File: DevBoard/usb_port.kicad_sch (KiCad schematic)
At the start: 134 parts, among them J401 TYPE-C 16PCB1.6 IP68, J402 I2CC logic analyzer, Q401 PGQ04N070, Q402 PGQ04N070, Q403 AO3401A, Q404 AO3401A, Q405 AO3400A, Q406 AO3400A, Q407 PGQ04N070, Q408 PGQ04N070, U401 TPS25751DREFR, U402 M24512-DFMC6TG, U403 BQ25756RRVR, U404 TPS62933DRLR, U405 TPD4S201TRGRRQ1

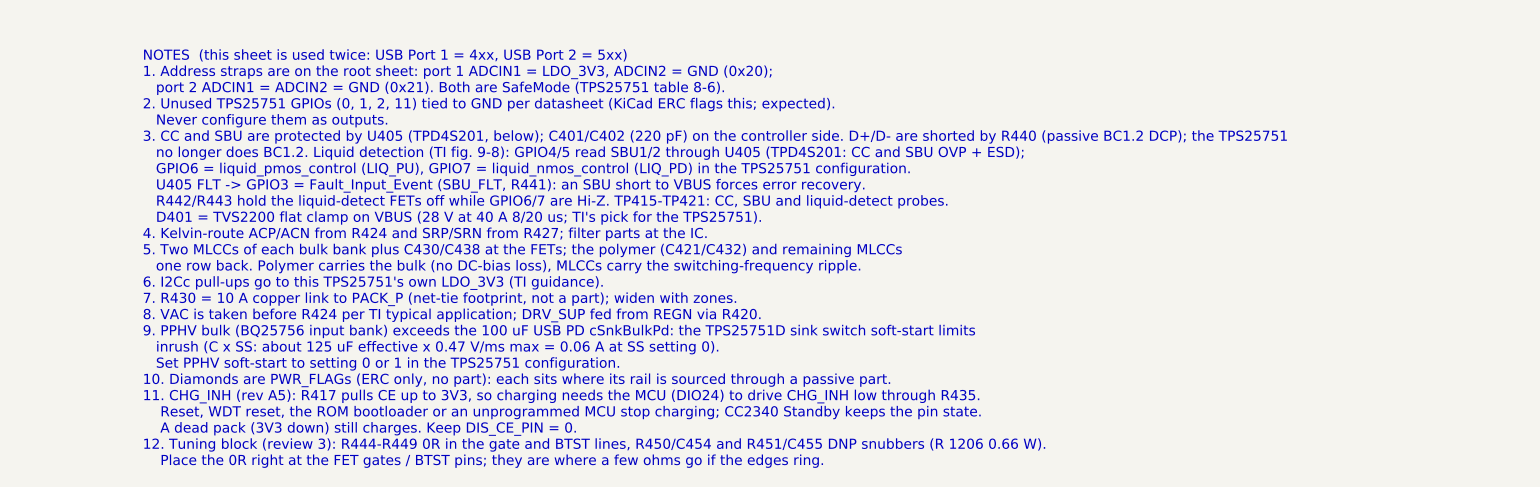
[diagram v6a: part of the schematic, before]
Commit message: Dev board: hybrid battery-side bulk, ship mode at 5 % SOC, CC2340 in stock
- C432/C532 (battery-side bulk, the only bulk cap biased in idle) ->
  Panasonic EEH-ZA1E101XP hybrid polymer (C264047), CP_Elec_6.3x7.7.
  Same 100 uF / 30 mOhm as the JIERR solid polymer, but leakage limit
  0.01CV = 25 uA instead of 0.2CV = 500 uA. +$1.28 per board. README
  item 43; review 4 B-4 closed. Board synced: 0 parity issues, no
  courtyard overlaps.
- Ship mode also triggers at RSOC <= 5 % (checklist, power states,
  review 4 S-1).
- CC2340R5MODA is in stock at TI.com (seen logged in, 2026-10-15):
  U301 Sourcing, bom_cost.py, checklist and README notes updated.

Co-Authored-By: Claude Opus 5.5 <noreply@anthropic.com>
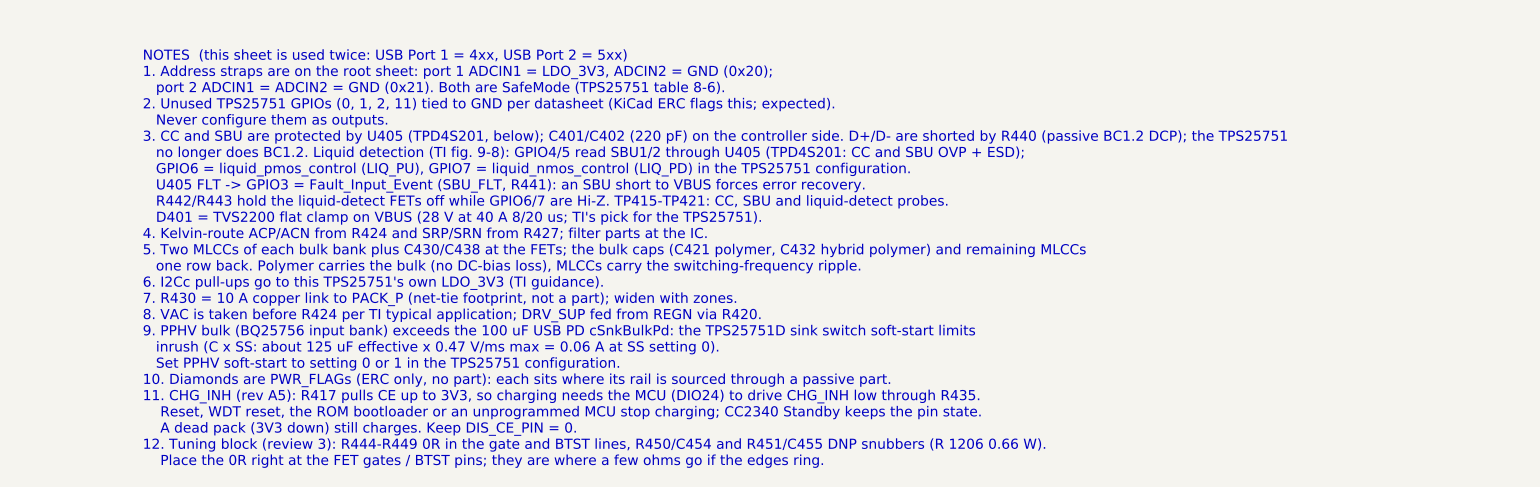
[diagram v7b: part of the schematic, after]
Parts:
- C432: footprint Capacitor_SMD:CP_Elec_6.3x5.8 -> Capacitor_SMD:CP_Elec_6.3x7.7; LCSC C46550465 -> C264047; MPN JIERR MA25V100M6x6 (polymer) -> Panasonic EEH-ZA1E101XP (hybrid polymer); Notes Battery-side bulk: solid polymer, no DC-bias loss (100 uF a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 -> Battery-side bulk (C432/C532): Panasonic ZA hybrid polymer 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
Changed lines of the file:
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@@
 		)
 	)
-	(text "NOTES  (this sheet is used twice: USB Port 1 = 4xx, USB Port 2 = 5xx)\n1. Address straps are on the root sheet: port 1 ADCIN1 = LDO_3V3, ADCIN2 = GND (0x20);\n   port 2 ADCIN1 = ADCIN2 = GND (0x21). Both are SafeMode (TPS25751 table 8-6).\n2. Unused TPS25751 GPIOs (0, 1, 2, 11) tied to GND per datasheet (KiCad ERC flags this; expected).\n   Never configure them as outputs.\n3. CC and SBU are protected by U405 (TPD4S201, below); C401/C402 (220 pF) on the controller side. D+/D- are shorted by R440 (passive BC1.2 DCP); the TPS25751\n   no longer does BC1.2. Liquid detection (TI fig. 9-8): GPIO4/5 read SBU1/2 through U405 (TPD4S201: CC and SBU OVP + ESD);\n   GPIO6 = liquid_pmos_control (LIQ_PU), GPIO7 = liquid_nmos_control (LIQ_PD) in the TPS25751 configuration.\n   U405 FLT -> GPIO3 = Fault_Input_Event (SBU_FLT, R441): an SBU short to VBUS forces error recovery.\n   R442/R443 hold the liquid-detect FETs off while GPIO6/7 are Hi-Z. TP415-TP421: CC, SBU and liquid-detect probes.\n   D401 = TVS2200 flat clamp on VBUS (28 V at 40 A 8/20 us; TI's pick for the TPS25751).\n4. Kelvin-route ACP/ACN from R424 and SRP/SRN from R427; filter parts at the IC.\n5. Two MLCCs of each bulk bank plus C430/C438 at the FETs; the polymer (C421/C432) and remaining MLCCs\n   one row back. Polymer carries the bulk (no DC-bias loss), MLCCs carry the switching-frequency ripple.\n6. I2Cc pull-ups go to this TPS25751's own LDO_3V3 (TI guidance).\n7. R430 = 10 A copper link to PACK_P (net-tie footprint, not a part); widen with zones.\n8. VAC is taken before R424 per TI typical application; DRV_SUP fed from REGN via R420.\n9. PPHV bulk (BQ25756 input bank) exceeds the 100 uF USB PD cSnkBulkPd: the TPS25751D sink switch soft-start limits\n   inrush (C x SS: about 125 uF effective x 0.47 V/ms max = 0.06 A at SS setting 0).\n   Set PPHV soft-start to setting 0 or 1 in the TPS25751 configuration.\n10. Diamonds are PWR_FLAGs (ERC only, no part): each sits where its rail is sourced through a passive part.\n11. CHG_INH (rev A5): R417 pulls CE up to 3V3, so charging needs the MCU (DIO24) to drive CHG_INH low through R435.\n    Reset, WDT reset, the ROM bootloader or an unprogrammed MCU stop charging; CC2340 Standby keeps the pin state.\n    A dead pack (3V3 down) still charges. Keep DIS_CE_PIN = 0.\n12. Tuning block (review 3): R444-R449 0R in the gate and BTST lines, R450/C454 and R451/C455 DNP snubbers (R 1206 0.66 W).\n    Place the 0R right at the FET gates / BTST pins; they are where a few ohms go if the edges ring."
+	(text "NOTES  (this sheet is used twice: USB Port 1 = 4xx, USB Port 2 = 5xx)\n1. Address straps are on the root sheet: port 1 ADCIN1 = LDO_3V3, ADCIN2 = GND (0x20);\n   port 2 ADCIN1 = ADCIN2 = GND (0x21). Both are SafeMode (TPS25751 table 8-6).\n2. Unused TPS25751 GPIOs (0, 1, 2, 11) tied to GND per datasheet (KiCad ERC flags this; expected).\n   Never configure them as outputs.\n3. CC and SBU are protected by U405 (TPD4S201, below); C401/C402 (220 pF) on the controller side. D+/D- are shorted by R440 (passive BC1.2 DCP); the TPS25751\n   no longer does BC1.2. Liquid detection (TI fig. 9-8): GPIO4/5 read SBU1/2 through U405 (TPD4S201: CC and SBU OVP + ESD);\n   GPIO6 = liquid_pmos_control (LIQ_PU), GPIO7 = liquid_nmos_control (LIQ_PD) in the TPS25751 configuration.\n   U405 FLT -> GPIO3 = Fault_Input_Event (SBU_FLT, R441): an SBU short to VBUS forces error recovery.\n   R442/R443 hold the liquid-detect FETs off while GPIO6/7 are Hi-Z. TP415-TP421: CC, SBU and liquid-detect probes.\n   D401 = TVS2200 flat clamp on VBUS (28 V at 40 A 8/20 us; TI's pick for the TPS25751).\n4. Kelvin-route ACP/ACN from R424 and SRP/SRN from R427; filter parts at the IC.\n5. Two MLCCs of each bulk bank plus C430/C438 at the FETs; the bulk caps (C421 polymer, C432 hybrid polymer) and remaining MLCCs\n   one row back. Polymer carries the bulk (no DC-bias loss), MLCCs carry the switching-frequency ripple.\n6. I2Cc pull-ups go to this TPS25751's own LDO_3V3 (TI guidance).\n7. R430 = 10 A copper link to PACK_P (net-tie footprint, not a part); widen with zones.\n8. VAC is taken before R424 per TI typical application; DRV_SUP fed from REGN via R420.\n9. PPHV bulk (BQ25756 input bank) exceeds the 100 uF USB PD cSnkBulkPd: the TPS25751D sink switch soft-start limits\n   inrush (C x SS: about 125 uF effective x 0.47 V/ms max = 0.06 A at SS setting 0).\n   Set PPHV soft-start to setting 0 or 1 in the TPS25751 configuration.\n10. Diamonds are PWR_FLAGs (ERC only, no part): each sits where its rail is sourced through a passive part.\n11. CHG_INH (rev A5): R417 pulls CE up to 3V3, so charging needs the MCU (DIO24) to drive CHG_INH low through R435.\n    Reset, WDT reset, the ROM bootloader or an unprogrammed MCU stop charging; CC2340 Standby keeps the pin state.\n    A dead pack (3V3 down) still charges. Keep DIS_CE_PIN = 0.\n12. Tuning block (review 3): R444-R449 0R in the gate and BTST lines, R450/C454 and R451/C455 DNP snubbers (R 1206 0.66 W).\n    Place the 0R right at the FET gates / BTST pins; they are where a few ohms go if the edges ring."
 		(exclude_from_sim no)
 		(at 299.72 368.3 0)
@@
 			)
 		)
-		(property "Footprint" "Capacitor_SMD:CP_Elec_6.3x5.8"
+		(property "Footprint" "Capacitor_SMD:CP_Elec_6.3x7.7"
 			(at 475.945 118.11 0)
 			(hide yes)
@@
 			)
 		)
-		(property "Notes" "Battery-side bulk: solid polymer, no DC-bias loss (100 uF at 16.8 V vs ~12 uF per 47 uF 1210 MLCC); 30 mOhm, 2.65 A at 100 kHz; MLCCs C431/C434/C435 carry the HF ripple. Always biased from PACK_P: measure its leakage at bring-up"
+		(property "Notes" "Battery-side bulk (C432/C532): Panasonic ZA hybrid polymer (conductive polymer + liquid electrolyte). 100 uF with no DC-bias loss, 30 mOhm and 2 A at 100 kHz like the solid polymer it replaced, but leakage <= 0.01CV = 25 uA max (the JIERR solid polymer was 0.2CV = 500 uA). It is the only bulk cap biased in idle (from PACK_P whenever the gauge FETs are on), so its leakage is idle drain. 10,000 h at 105 C. MLCCs C431/C434/C435 carry the HF ripple"
 			(at 474.98 121.92 0)
 			(hide yes)
@@
 			)
 		)
-		(property "LCSC" "C46550465"
+		(property "LCSC" "C264047"
 			(at 474.98 121.92 0)
 			(hide yes)
@@
 			)
 		)
-		(property "MPN" "JIERR MA25V100M6x6 (polymer)"
+		(property "MPN" "Panasonic EEH-ZA1E101XP (hybrid polymer)"
 			(at 474.98 121.92 0)
 			(hide yes)

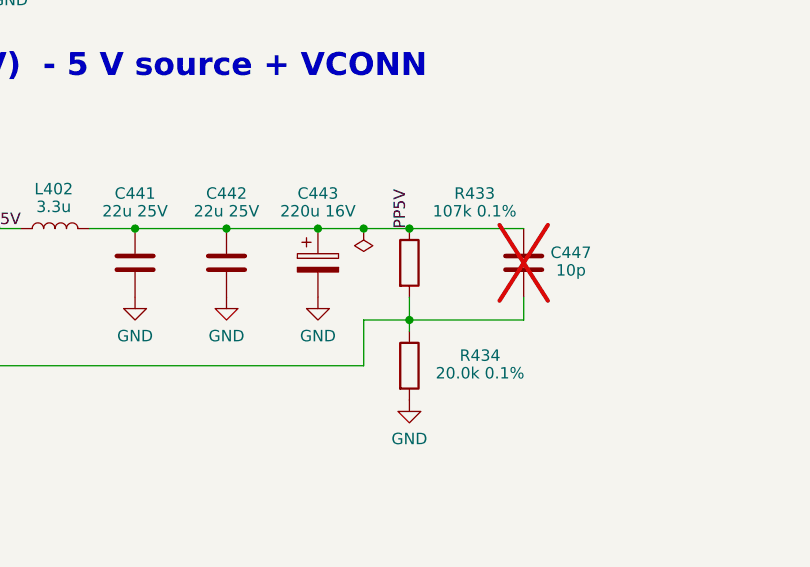
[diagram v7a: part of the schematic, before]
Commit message: Dev board: cut JLC extended parts 37 -> 27 for a 2-board build
tools/bom_fee_cut.py (one-shot); README item 44. At 2 boards the costed
BOM goes from $124.28 to $108.49 per board.
- Basic/preferred swaps, no footprint changes: C313 -> C1548, C315/C314
  -> C1550, C401/C402 -> C1530 (X7R), R433/R434 -> 120k/22k 1 %
  (PP5V 5.16 V), C443/C543 -> 100 uF 35 V Honor polymer (same as C421).
- Hand-fit from LCSC: BT101-BT104, the 13 Harwin test loops, U202, D105
  (dev-only; out of the position file).
- Board: fields refreshed by netlist_to_board.py; also includes Logan's
  block move made in KiCad. DRC parity 0; ERC unchanged.

Co-Authored-By: Claude Opus 5.5 <noreply@anthropic.com>
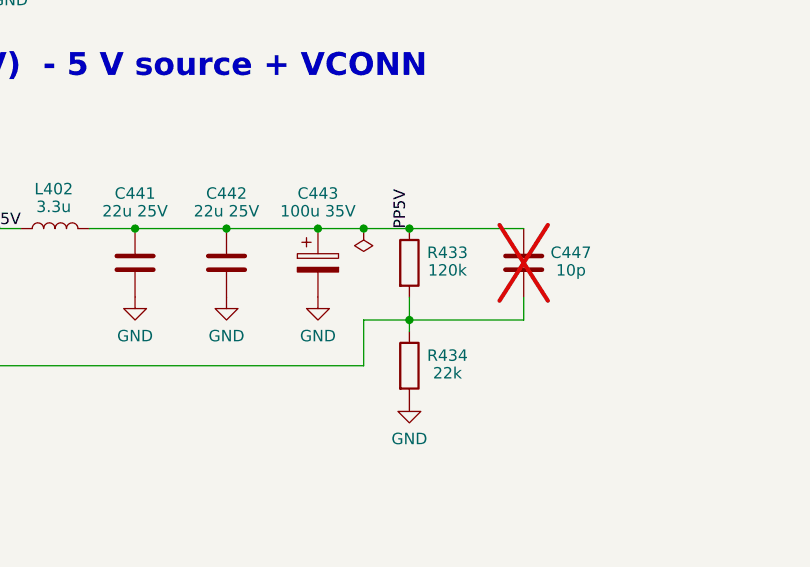
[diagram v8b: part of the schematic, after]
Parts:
- C401, C402: LCSC C307445 -> C1530; MPN CL05C221JB5NNNC -> 0402B221K500NT; Notes 50V C0G. 220 pF: with the TPD4S201's 40-120 pF the CC total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 -> 50V X7R (JLC basic). 220 pF: with the TPD4S201's 40-120 pF 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
- C443: value 220u 16V -> 100u 35V; LCSC C25503905 -> C5246554; MPN ChuangHui SS221M160E7R7R4Z00ZZ (polymer) -> Honor Elec HV1V107M0607PZ (polymer); Notes PP5V bulk: USB PD cSrcBulkShared needs 120 uF; polymer has 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 -> PP5V bulk: USB PD cSrcBulkShared needs 120 uF: 100 uF polym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
- R433: value 107k 0.1% -> 120k; LCSC C865130 -> C17436; MPN RT0805BRD07107KL -> 0805W8F1203T5E; Notes PP5V = 0.8 x (1 + 107/20) = 5.08 V: margin over the TPS2575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 -> PP5V = 0.8 x (1 + 120/22) = 5.16 V (1 % basic parts since 2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
- R434: value 20.0k 0.1% -> 22k; LCSC C469660 -> C17560; MPN RT0805BRD0720KL -> 0805W8F2202T5E
- TP405, TP406, TP412: LCSC C55121754 -> (none); Sourcing (none) -> Hand-solder, not JLC assembled (test loop, dev only; saves 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
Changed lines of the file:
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@@
 			)
 		)
-		(property "Value" "220u 16V"
+		(property "Value" "100u 35V"
 			(at 157.48 201.27 0)
 			(show_name no)
@@
 			)
 		)
-		(property "Notes" "PP5V bulk: USB PD cSrcBulkShared needs 120 uF; polymer has no DC-bias loss"
+		(property "Notes" "PP5V bulk: USB PD cSrcBulkShared needs 120 uF: 100 uF polymer (no DC-bias loss) + C441/C442 2 x 22 uF. Same part as C421 since 2026-10-15 (was a 220 uF 16 V polymer) to save a JLC extended-part fee"
 			(at 0 0 0)
 			(hide yes)
@@
 			)
 		)
-		(property "LCSC" "C25503905"
+		(property "LCSC" "C5246554"
 			(at 157.48 207.01 0)
 			(hide yes)
@@
 			)
 		)
-		(property "MPN" "ChuangHui SS221M160E7R7R4Z00ZZ (polymer)"
+		(property "MPN" "Honor Elec HV1V107M0607PZ (polymer)"
 			(at 157.48 207.01 0)
 			(hide yes)
@@
 		(dnp no)
 		(property "Reference" "R434"
-			(at 175.49 217.31 0)
+			(at 171.87 217.31 0)
 			(show_name no)
 			(do_not_autoplace no)
@@
 			)
 		)
-		(property "Value" "20.0k 0.1%"
-			(at 175.49 219.27 0)
+		(property "Value" "22k"
+			(at 171.87 219.27 0)
 			(show_name no)
 			(do_not_autoplace no)
@@
 			)
 		)
-		(property "LCSC" "C469660"
+		(property "LCSC" "C17560"
 			(at 167.64 218.44 0)
 			(hide yes)
@@
 			)
 		)
-		(property "MPN" "RT0805BRD0720KL"
+		(property "MPN" "0805W8F2202T5E"
 			(at 167.64 218.44 0)
 			(hide yes)
@@
 		(in_bom yes)
 		(on_board yes)
-		(in_pos_files yes)
+		(in_pos_files no)
 		(dnp no)
 		(property "Reference" "TP405"
@@
 			)
 		)
-		(property "LCSC" "C55121754"
+		(property "LCSC" ""
 			(at 106.68 289.56 0)
 			(hide yes)
@@
 			)
 		)
+		(property "Sourcing" "Hand-solder, not JLC assembled (test loop, dev only; saves a JLC extended-part fee; LCSC C55121754 RH-S2761-46R (ronghe; Harwin S2761-46R equivalent))"
+			(at 106.68 289.56 0)
+			(hide yes)
+			(show_name no)
+			(do_not_autoplace no)
+			(effects
+				(font
+					(size 1.27 1.27)
+				)
+			)
+		)
 		(pin "1"
 		)
@@
 		(dnp no)
 		(property "Reference" "R433"
-			(at 174.89 199.30 0)
+			(at 171.87 205.88 0)
 			(show_name no)
 			(do_not_autoplace no)
@@
 			)
 		)
-		(property "Value" "107k 0.1%"
-			(at 174.89 201.27 0)
+		(property "Value" "120k"
+			(at 171.87 207.84 0)
 			(show_name no)
 			(do_not_autoplace no)
@@
 			)
 		)
-		(property "LCSC" "C865130"
+		(property "LCSC" "C17436"
 			(at 167.64 207.01 0)
 			(hide yes)
@@
 			)
 		)
-		(property "MPN" "RT0805BRD07107KL"
+		(property "MPN" "0805W8F1203T5E"
 			(at 167.64 207.01 0)
 			(hide yes)
@@
 			)
 		)
-		(property "Notes" "PP5V = 0.8 x (1 + 107/20) = 5.08 V: margin over the TPS25751 4.9 V minimum (review m4)"
+		(property "Notes" "PP5V = 0.8 x (1 + 120/22) = 5.16 V (1 % basic parts since 2026-10-15; was 107k/20.0k 0.1 % for 5.08 V): inside the TPS25751's 4.9-5.5 V PP5V range and USB vSafe5V"
 			(at 167.64 207.01 0)
 			(hide yes)
@@
 			)
 		)
-		(property "Notes" "50V C0G. 220 pF: with the TPD4S201's 40-120 pF the CC total stays under the TPS25751's 480 pF (TI EVM value with this protector; review 4 C-3)"
+		(property "Notes" "50V X7R (JLC basic). 220 pF: with the TPD4S201's 40-120 pF the CC total stays under the TPS25751's 480 pF (TI EVM value with this protector; review 4 C-3)"
 			(at 119.38 93.98 0)
 			(hide yes)
@@
 			)
 		)
-		(property "LCSC" "C307445"
+		(property "LCSC" "C1530"
 			(at 119.38 93.98 0)
 			(hide yes)
@@
 			)
 		)
-		(property "MPN" "CL05C221JB5NNNC"
+		(property "MPN" "0402B221K500NT"
 			(at 119.38 93.98 0)
 			(hide yes)
@@
 			)
 		)
-		(property "Notes" "50V C0G. 220 pF: with the TPD4S201's 40-120 pF the CC total stays under the TPS25751's 480 pF (TI EVM value with this protector; review 4 C-3)"
+		(property "Notes" "50V X7R (JLC basic). 220 pF: with the TPD4S201's 40-120 pF the CC total stays under the TPS25751's 480 pF (TI EVM value with this protector; review 4 C-3)"
 			(at 111.76 93.98 0)
 			(hide yes)
@@
 			)
 		)
-		(property "LCSC" "C307445"
+		(property "LCSC" "C1530"
 			(at 111.76 93.98 0)
 			(hide yes)
@@
 			)
 		)
-		(property "MPN" "CL05C221JB5NNNC"
+		(property "MPN" "0402B221K500NT"
 			(at 111.76 93.98 0)
 			(hide yes)
@@
 		(in_bom yes)
 		(on_board yes)
-		(in_pos_files yes)
+		(in_pos_files no)
 		(dnp no)
 		(property "Reference" "TP406"
@@
 			)
 		)
-		(property "LCSC" "C55121754"
+		(property "LCSC" ""
 			(at 121.92 289.56 0)
 			(hide yes)
@@
 			)
 		)
+		(property "Sourcing" "Hand-solder, not JLC assembled (test loop, dev only; saves a JLC extended-part fee; LCSC C55121754 RH-S2761-46R (ronghe; Harwin S2761-46R equivalent))"
+			(at 121.92 289.56 0)
+			(hide yes)
+			(show_name no)
+			(do_not_autoplace no)
+			(effects
+				(font
+					(size 1.27 1.27)
+				)
+			)
+		)
 		(pin "1"
 		)
@@
 		(in_bom yes)
 		(on_board yes)
-		(in_pos_files yes)
+		(in_pos_files no)
 		(dnp no)
 		(property "Reference" "TP412"
@@
 			)
 		)
-		(property "LCSC" "C55121754"
+		(property "LCSC" ""
 			(at 213.36 289.56 0)
 			(hide yes)
@@
 			(at 213.36 289.56 0)
 			(hide yes)
+			(show_name no)
+			(do_not_autoplace no)
+			(effects
+				(font
+					(size 1.27 1.27)
+				)
+			)
+		)
+		(property "Sourcing" "Hand-solder, not JLC assembled (test loop, dev only; saves a JLC extended-part fee; LCSC C55121754 RH-S2761-46R (ronghe; Harwin S2761-46R equivalent))"
+			(at 213.36 289.56 0)
+			(hide yes)
